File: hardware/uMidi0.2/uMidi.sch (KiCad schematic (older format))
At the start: 42 parts, among them CON1 USB-MINI-B, IC1 6N138, IC2 ATXMEGA128A4U-M, P1 MIDI In, P2 MIDI Thru, P3 MIDI T/O, P4 MIDI Out, P5 5..12 V, P6 PDI, P7 GPIO1, P8 GPIO2, P9 GPIO2, U1 74LS14, U2 LT1129CST-3.3, X1 32MHz

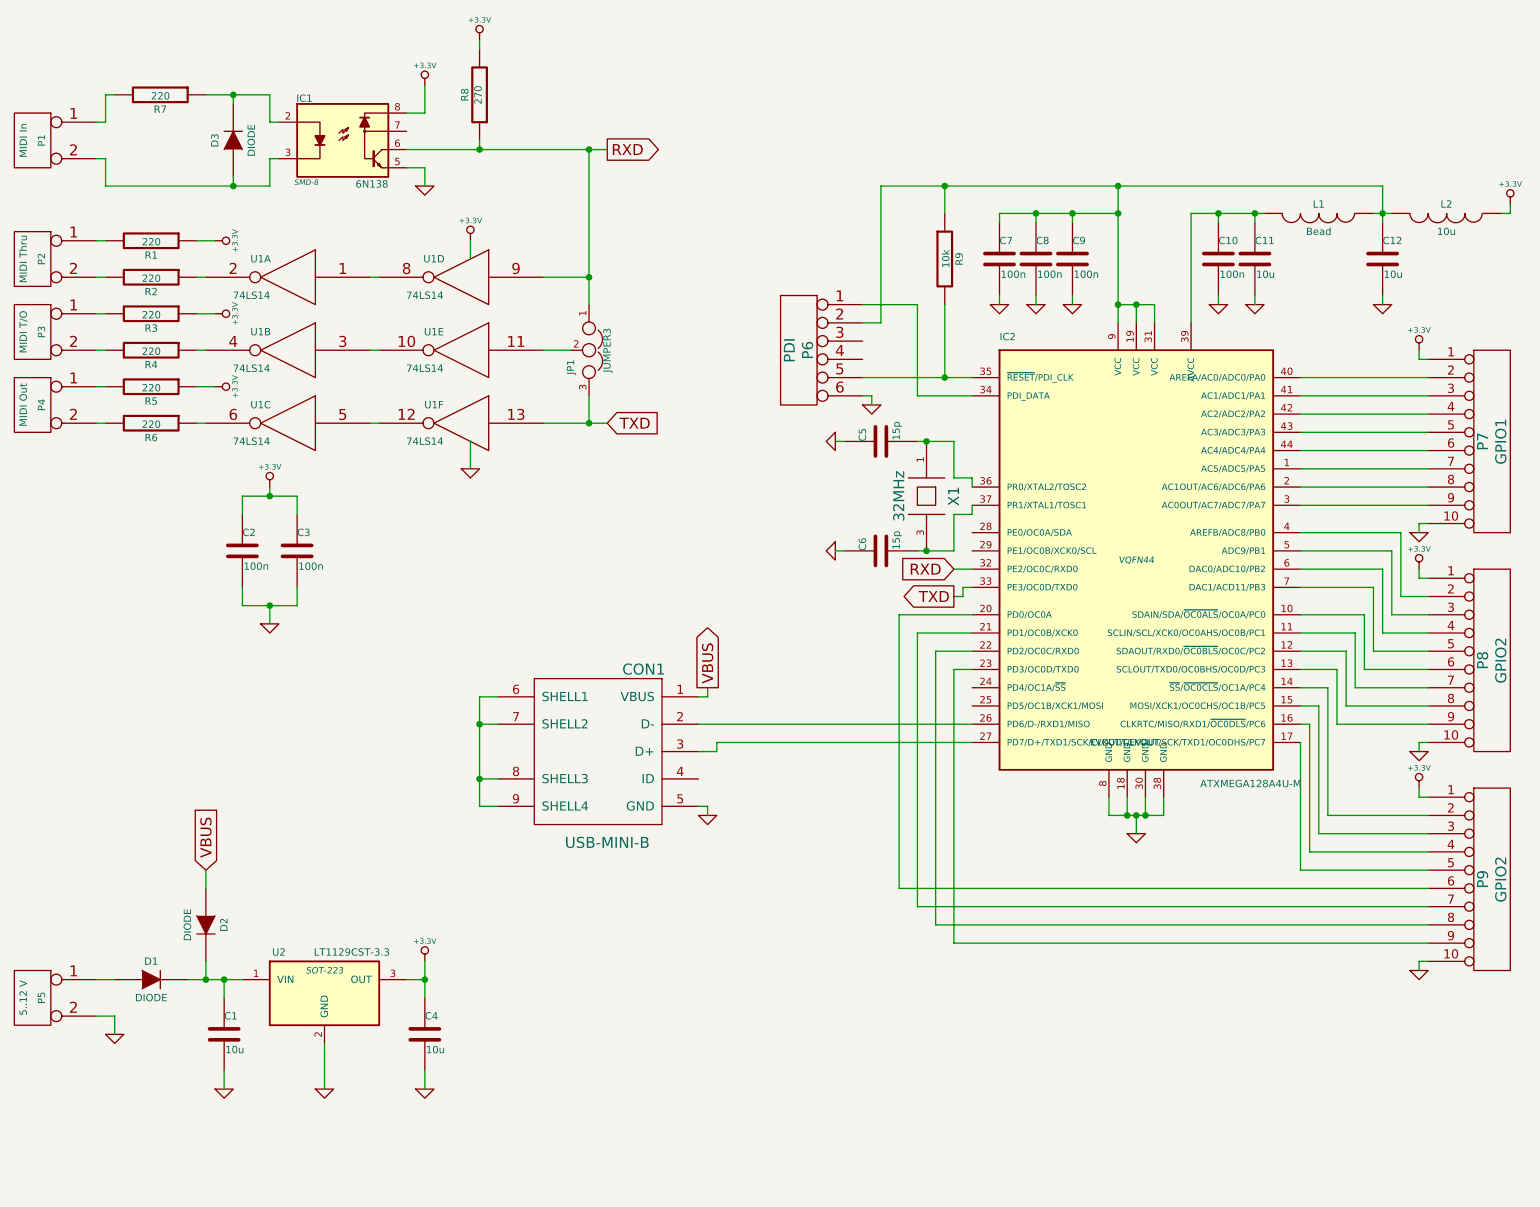
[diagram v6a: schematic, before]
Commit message: Add tvs diodes to usb voltage and data
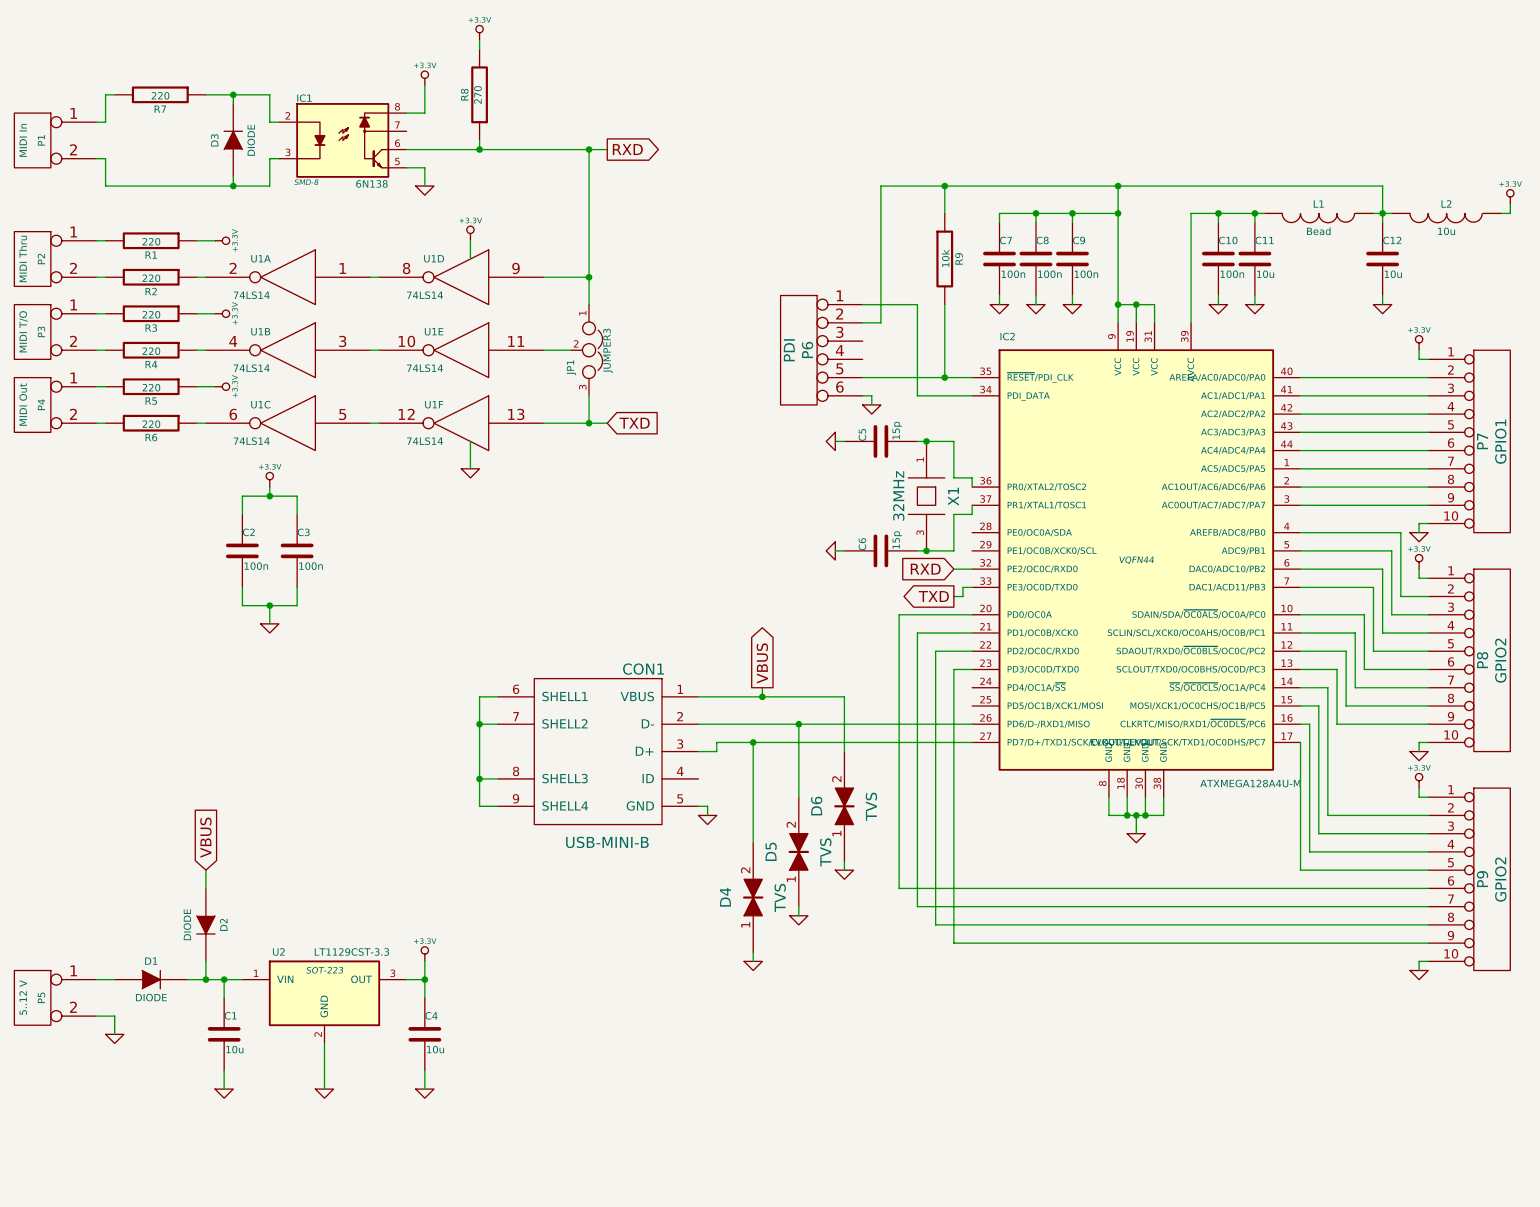
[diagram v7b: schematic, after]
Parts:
- added D4, D5, D6: TVS, symbol TVS
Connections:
- net GND: now also D4.1, D5.1, D6.1
- net VBUS: now also D6.2
- net at CON1.2 (D-), IC2.26 (PD6/D-/RXD1/MISO): now also D5.2
- net at CON1.3 (D+), IC2.27 (PD7/D+/TXD1/SCK/CLKOUT/EVOUT): now also D4.2

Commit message: Add cap to usb voltage
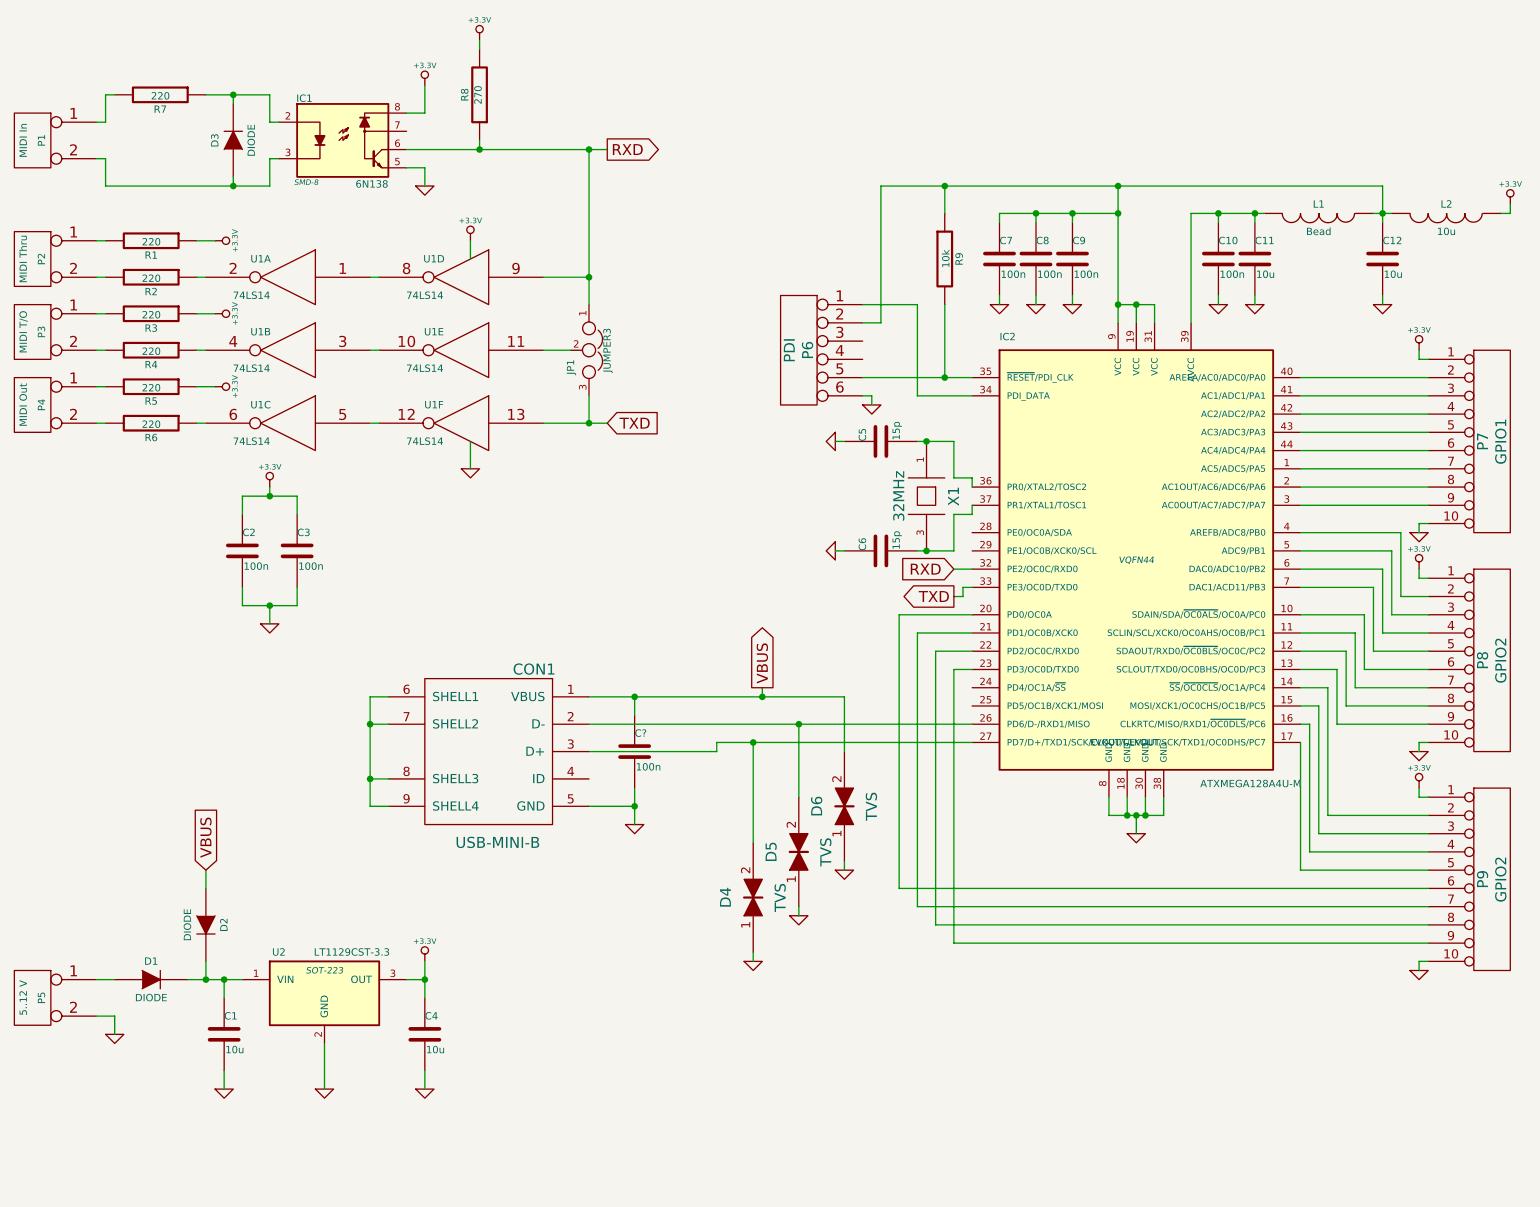
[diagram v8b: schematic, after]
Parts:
- added C?: 100n, symbol C
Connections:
- net GND: now also C?.2
- net VBUS: now also C?.1
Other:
- moved on the sheet: CON1
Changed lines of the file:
@@
 	7200 5150 7200 5250
 Wire Wire Line
-	7050 5150 7150 5150
-Wire Wire Line
-	7150 5150 7200 5150
-Wire Wire Line
-	7200 5150 7250 5150
-Wire Wire Line
-	7250 5150 7350 5150
+	7050 5150 7350 5150
 Wire Wire Line
 	7350 5150 7350 5050
@@
 	7200 2350 7200 2450
 Wire Wire Line
-	7100 2350 7200 2350
-Wire Wire Line
-	7200 2350 7300 2350
+	7100 2350 7300 2350
 Connection ~ 7200 2350
 Wire Wire Line
@@
 	5800 2450 5700 2450
 Wire Wire Line
-	5700 2750 6150 2750
-Wire Wire Line
-	6150 2750 6300 2750
+	5700 2750 6300 2750
 Connection ~ 6150 2750
 Wire Wire Line
@@
 	3550 2100 3550 2000
 Wire Wire Line
-	3950 3000 4200 3000
-Wire Wire Line
-	4200 3000 4300 3000
-Wire Wire Line
-	4900 4750 5100 4750
-Wire Wire Line
-	5100 4750 6300 4750
-Wire Wire Line
-	4800 4650 5350 4650
-Wire Wire Line
-	5350 4650 6300 4650
+	3950 3000 4300 3000
+Wire Wire Line
+	4900 4750 6300 4750
+Wire Wire Line
+	4200 4650 6300 4650
 $Comp
 L USB-MINI-B CON1
 U 1 1 53C6D9DB
-P 4250 4800
-F 0 "CON1" H 4000 5250 60  0000 C CNN
-F 1 "USB-MINI-B" H 4200 4300 60  0000 C CNN
-F 2 "" H 4250 4800 60  0000 C CNN
-F 3 "" H 4250 4800 60  0000 C CNN
-	1    4250 4800
+P 3650 4800
+F 0 "CON1" H 3400 5250 60  0000 C CNN
+F 1 "USB-MINI-B" H 3600 4300 60  0000 C CNN
+F 2 "" H 3650 4800 60  0000 C CNN
+F 3 "" H 3650 4800 60  0000 C CNN
+	1    3650 4800
 	-1   0    0    -1
 $EndComp
 Wire Wire Line
-	3700 4500 3600 4500
-Wire Wire Line
-	3600 4500 3600 4650
-Wire Wire Line
-	3600 4650 3600 4950
-Wire Wire Line
-	3600 4950 3600 5100
-Wire Wire Line
-	3600 5100 3700 5100
-Wire Wire Line
-	3700 4950 3600 4950
-Connection ~ 3600 4950
-Wire Wire Line
-	3700 4650 3600 4650
-Connection ~ 3600 4650
+	3100 4500 3000 4500
+Wire Wire Line
+	3000 4500 3000 5100
+Wire Wire Line
+	3000 5100 3100 5100
+Wire Wire Line
+	3100 4950 3000 4950
+Connection ~ 3000 4950
+Wire Wire Line
+	3100 4650 3000 4650
+Connection ~ 3000 4650
 $Comp
 L GND #PWR16
 U 1 1 53C6DAEC
-P 4850 5150
-F 0 "#PWR16" H 4850 5150 30  0001 C CNN
-F 1 "GND" H 4850 5080 30  0001 C CNN
-F 2 "" H 4850 5150 60  0000 C CNN
-F 3 "" H 4850 5150 60  0000 C CNN
-	1    4850 5150
+P 4450 5200
+F 0 "#PWR16" H 4450 5200 30  0001 C CNN
+F 1 "GND" H 4450 5130 30  0001 C CNN
+F 2 "" H 4450 5200 60  0000 C CNN
+F 3 "" H 4450 5200 60  0000 C CNN
+	1    4450 5200
 	1    0    0    -1
 $EndComp
@@
 Connection ~ 4200 3000
 Wire Wire Line
-	4200 1500 4200 2200
-Wire Wire Line
-	4200 2200 4200 2350
+	4200 1500 4200 2350
 Wire Wire Line
 	4200 2200 3950 2200
@@
 $EndComp
 Wire Wire Line
-	1550 1700 2250 1700
-Wire Wire Line
-	2250 1700 2450 1700
+	1550 1700 2450 1700
 Wire Wire Line
 	2450 1700 2450 1550
@@
 Connection ~ 2250 1700
 Wire Wire Line
-	2100 1200 2250 1200
-Wire Wire Line
-	2250 1200 2450 1200
+	2100 1200 2450 1200
 Wire Wire Line
 	2450 1200 2450 1350
@@
 $EndComp
 Wire Wire Line
-	3200 1500 3600 1500
-Wire Wire Line
-	3600 1500 4200 1500
-Wire Wire Line
-	4200 1500 4300 1500
+	3200 1500 4300 1500
 Wire Wire Line
 	3600 1500 3600 1450
@@
 	7500 1850 7500 2450
 Wire Wire Line
-	7500 1850 7650 1850
-Wire Wire Line
-	7650 1850 7850 1850
-Wire Wire Line
-	7850 1850 7900 1850
+	7500 1850 7900 1850
 Wire Wire Line
 	7850 1900 7850 1850
@@
 $EndComp
 Wire Wire Line
-	6450 1850 6650 1850
-Wire Wire Line
-	6650 1850 6850 1850
-Wire Wire Line
-	6850 1850 7100 1850
-Wire Wire Line
-	7100 1700 7100 1850
-Wire Wire Line
-	7100 1850 7100 2350
-Wire Wire Line
-	7100 2350 7100 2450
+	6450 1850 7100 1850
+Wire Wire Line
+	7100 1700 7100 2450
 Wire Wire Line
 	6850 2350 6850 2300
@@
 	9250 1850 9250 1800
 Wire Wire Line
-	8500 1850 8550 1850
-Wire Wire Line
-	8550 1850 8600 1850
-Wire Wire Line
-	8550 1700 8550 1850
-Wire Wire Line
-	8550 1850 8550 1900
+	8500 1850 8600 1850
+Wire Wire Line
+	8550 1700 8550 1900
 Connection ~ 8550 1850
 Wire Wire Line
-	5800 1700 6150 1700
-Wire Wire Line
-	6150 1700 7100 1700
-Wire Wire Line
-	7100 1700 8550 1700
+	5800 1700 8550 1700
 Wire Wire Line
 	6150 1700 6150 1850
@@
 	2100 5950 2100 6050
 Wire Wire Line
-	2000 6050 2100 6050
-Wire Wire Line
-	2100 6050 2200 6050
-Wire Wire Line
-	2200 6050 2300 6050
+	2000 6050 2300 6050
 $Comp
 L GND #PWR8
@@
 	3300 6650 3300 6550
 Wire Wire Line
-	3300 5950 3300 6050
-Wire Wire Line
-	3300 6050 3300 6150
+	3300 5950 3300 6150
 Wire Wire Line
 	3300 6050 3200 6050
@@
 	2300 3500 2300 3400
 Wire Wire Line
-	2300 3400 2450 3400
-Wire Wire Line
-	2450 3400 2600 3400
+	2300 3400 2600 3400
 Wire Wire Line
 	2600 3400 2600 3500
 Wire Wire Line
-	2300 4000 2450 4000
-Wire Wire Line
-	2450 4000 2600 4000
+	2300 4000 2600 4000
 Wire Wire Line
 	2600 4000 2600 3900
@@
 	8100 5450 8800 5450
 Wire Wire Line
-	4900 4750 4900 4800
-Wire Wire Line
-	4900 4800 4800 4800
-Wire Wire Line
-	4850 5150 4850 5100
-Wire Wire Line
-	4850 5100 4800 5100
-Wire Wire Line
-	4800 4500 5150 4500
-Wire Wire Line
-	5150 4500 5600 4500
+	4900 4800 4900 4750
+Wire Wire Line
+	4200 4800 4900 4800
+Wire Wire Line
+	4200 5100 4450 5100
+Wire Wire Line
+	4200 4500 5600 4500
 Wire Wire Line
 	5150 4500 5150 4450
@@
 	6250 3900 6300 3900
 Wire Wire Line
-	6000 3700 6050 3700
-Wire Wire Line
-	6050 3700 6200 3700
+	6000 3700 6200 3700
 Wire Wire Line
 	6200 3700 6200 3500
@@
 	6200 3300 6200 3100
 Wire Wire Line
-	6200 3100 6050 3100
-Wire Wire Line
-	6050 3100 6000 3100
+	6200 3100 6000 3100
 $Comp
 L C C6
@@
 Wire Wire Line
 	5600 4500 5600 4800
+$Comp
+L C C?
+U 1 1 53CD5DBF
+P 4450 4800
+F 0 "C?" H 4450 4900 40  0000 L CNN
+F 1 "100n" H 4456 4715 40  0000 L CNN
+F 2 "" H 4488 4650 30  0000 C CNN
+F 3 "" H 4450 4800 60  0000 C CNN
+	1    4450 4800
+	1    0    0    -1
+$EndComp
+Wire Wire Line
+	4450 5000 4450 5200
+Connection ~ 4450 5100
+Wire Wire Line
+	4450 4600 4450 4500
+Connection ~ 4450 4500
 $EndSCHEMATC
